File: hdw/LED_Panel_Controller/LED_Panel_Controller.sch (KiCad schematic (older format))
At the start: 0 parts

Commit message: lots of schematic progress
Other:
- note added: "14. Platform ETC"
- note removed: "14. Time of Flight"
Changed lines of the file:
@@
 encoding utf-8
 Sheet 1 34
-Title ""
-Date "2020-09-08"
-Rev ""
-Comp ""
+Title "LED Panel Controller"
+Date "2020-12-23"
+Rev "A"
+Comp "Drew Maatman, Logan Wedel"
 Comment1 ""
 Comment2 ""
@@
 S 3750 5420 500  150
 U 5F582A92
-F0 "Time of Flight" 50
-F1 "Time_of_Flight.sch" 50
+F0 "Platform ETC" 50
+F1 "Platform_ETC.sch" 50
 $EndSheet
 $Sheet
@@
 13. I2C Boost
 Text Notes 1290 5570 0    100  ~ 20
-14. Time of Flight
+14. Platform ETC
 Text Notes 1290 5920 0    100  ~ 20
 15. USB UART Bridge

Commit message: made a lot more schematic progress
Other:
- note added: "TODO:\n- Determine actual +12V current draw, reevaluate input protection circuit - 2A\n- Determine image size, external flash size- 16,384 bytes\n* Figure out screen modes/mode LEDs\n* Draw WiFi module sheet\n* What PIC32MZ SKU will we use? Should be highest memory + speed - Drew\n"
- note removed: "TODO:\n- Determine actual +12V current draw, reevaluate input protection circuit - 2A\n- Input EMI filter? - Drew\n- Determine image size, external flash size- 16,384 bytes\n- Determine +5V current draw, decide on converter - Drew - 3A\n- Determine +3.3V Current Draw, decide on converter - Drew\n- Remove high frequency PIC32MZ bypass caps - Drew\n- Figure out panel connectors - Drew\n* Figure out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"
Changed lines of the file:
@@
 33. Mechanical
 Text Notes 8660 6640 0    50   ~ 0
-TODO:\n- Determine actual +12V current draw, reevaluate input protection circuit - 2A\n- Input EMI filter? - Drew\n- Determine image size, external flash size- 16,384 bytes\n- Determine +5V current draw, decide on converter - Drew - 3A\n- Determine +3.3V Current Draw, decide on converter - Drew\n- Remove high frequency PIC32MZ bypass caps - Drew\n- Figure out panel connectors - Drew\n* Figure out panel level shifting - Logan\n- Figure out SPI flash circuit - Drew\n* Figure out screen modes/mode LEDs\n- Draw SD card sheet - Logan\n* Draw WiFi module sheet\n- Draw I2C boost sheet with LTC1694 - Drew\n* Determine what will be configurable, add hardstraps\n* What will pushbuttons do?\n* What PIC32MZ SKU will we use? Should be highest memory + speed - Drew\n- Change PGOOD LEDs sheet to use +3.3V_PGL global power symbol - Drew\n* Add USB Telemetry sheet\n
+TODO:\n- Determine actual +12V current draw, reevaluate input protection circuit - 2A\n- Determine image size, external flash size- 16,384 bytes\n* Figure out screen modes/mode LEDs\n* Draw WiFi module sheet\n* What PIC32MZ SKU will we use? Should be highest memory + speed - Drew\n
 $Sheet
 S 7030 5770 500  150

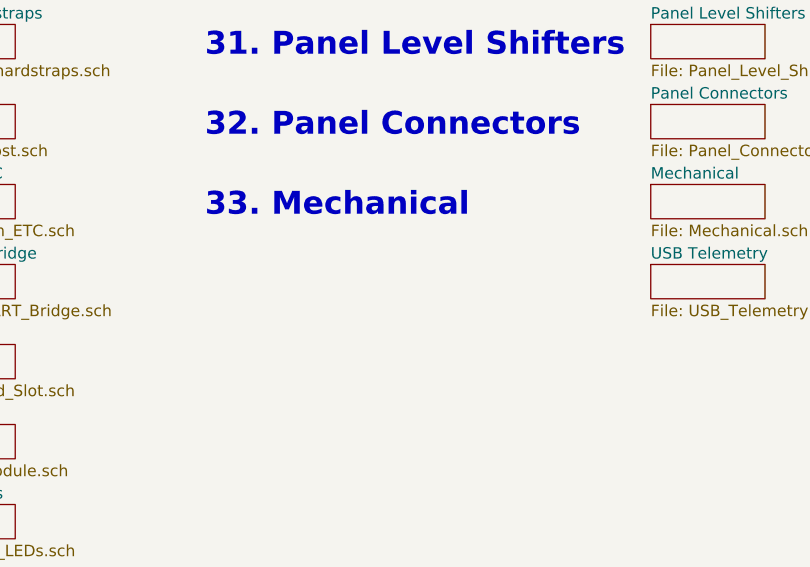
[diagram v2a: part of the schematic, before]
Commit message: fixed level shifter sheet
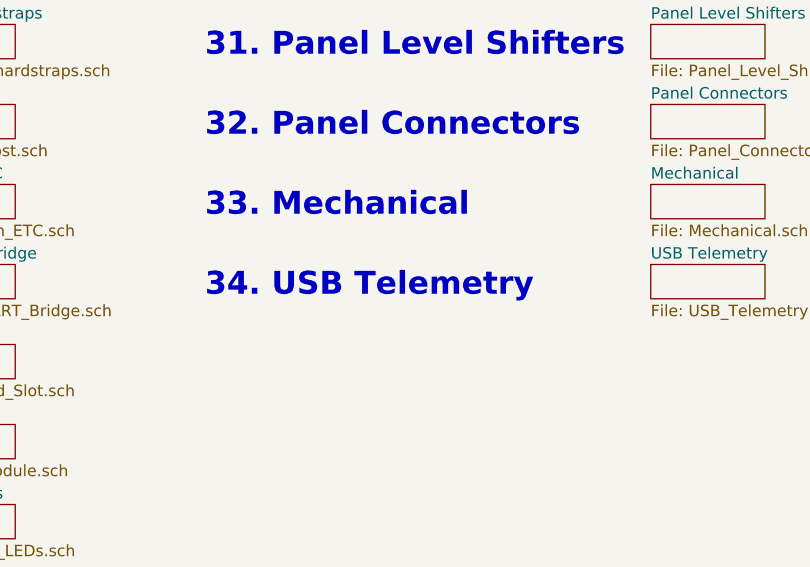
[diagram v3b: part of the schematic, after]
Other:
- note added: "34. USB Telemetry"
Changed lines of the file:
@@
 F1 "USB_Telemetry.sch" 50
 $EndSheet
+Text Notes 5080 5920 0    100  ~ 20
+34. USB Telemetry
 $EndSCHEMATC

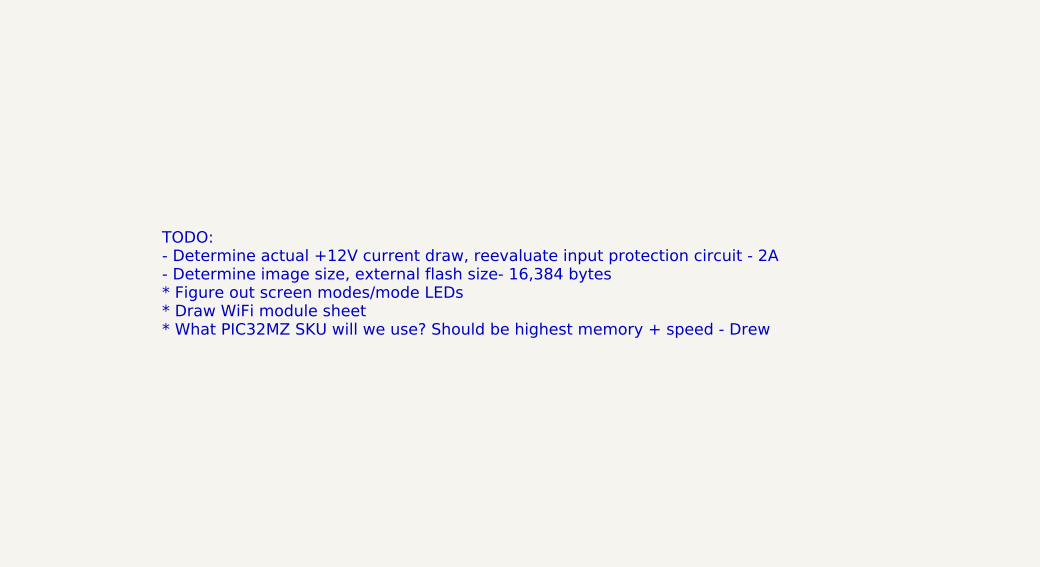
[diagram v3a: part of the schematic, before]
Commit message: lots of MCU pin assignments
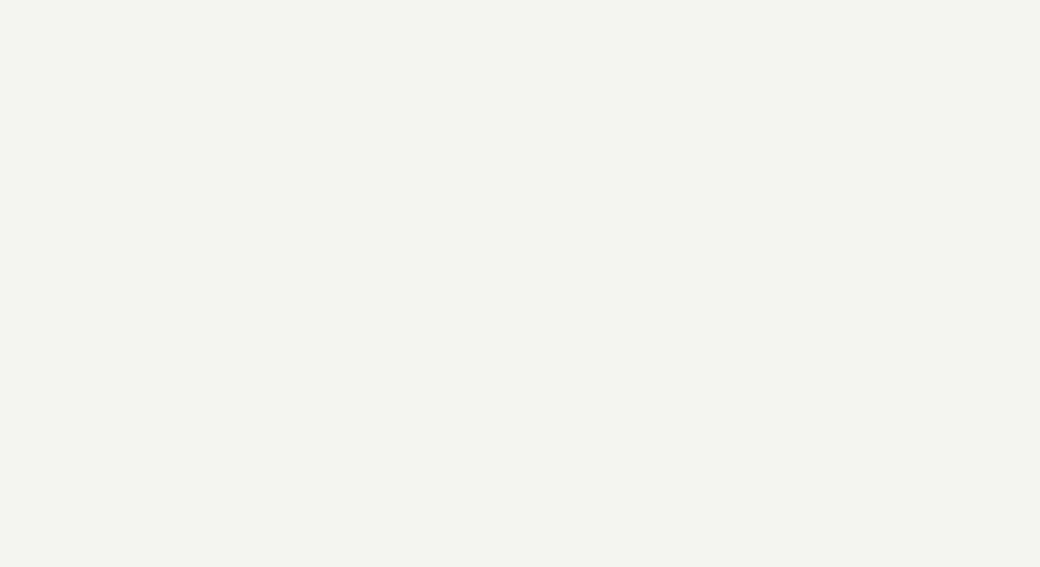
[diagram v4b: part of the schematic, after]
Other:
- note removed: "TODO:\n- Determine actual +12V current draw, reevaluate input protection circuit - 2A\n- Determine image size, external flash size- 16,384 bytes\n* Figure out screen modes/mode LEDs\n* Draw WiFi module sheet\n* What PIC32MZ SKU will we use? Should be highest memory + speed - Drew\n"
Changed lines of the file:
@@
 Text Notes 5080 5570 0    100  ~ 20
 33. Mechanical
-Text Notes 8660 6640 0    50   ~ 0
-TODO:\n- Determine actual +12V current draw, reevaluate input protection circuit - 2A\n- Determine image size, external flash size- 16,384 bytes\n* Figure out screen modes/mode LEDs\n* Draw WiFi module sheet\n* What PIC32MZ SKU will we use? Should be highest memory + speed - Drew\n
 $Sheet
 S 7030 5770 500  150

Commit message: more schematic development
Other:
- note added: "16. USB Telemetry"
- note added: "17. SD Card Slot"
- note added: "18. WiFi Module"
- note added: "19. PGOOD LEDs"
- note added: "20. Status LEDs"
- note added: "21. Backup RTC"
- note added: "22. Pushbuttons"
- note added: "23. Mode LEDs"
- note added: "24. SPI Flash 0"
- note added: "25. SPI Flash 1"
- note added: "26. SPI Flash 2"
- note added: "27. SPI Flash 3"
- note added: "28. SPI Flash 4"
- note added: "29. SPI Flash 5"
- note added: "30. SPI Flash 6"
- note added: "31. SPI Flash 7"
- note added: "32. Panel Level Shifters"
- note added: "33. Panel Connectors"
- note added: "34. Mechanical"
- note removed: "16. SD Card Slot"
- note removed: "17. WiFi Module"
- note removed: "18. PGOOD LEDs"
- note removed: "19. Status LEDs"
- note removed: "20. Backup RTC"
- note removed: "21. Pushbuttons"
- note removed: "22. Mode LEDs"
- note removed: "23. SPI Flash 0"
- note removed: "24. SPI Flash 1"
- note removed: "25. SPI Flash 2"
- note removed: "26. SPI Flash 3"
- note removed: "27. SPI Flash 4"
- note removed: "28. SPI Flash 5"
- note removed: "29. SPI Flash 6"
- note removed: "30. SPI Flash 7"
- note removed: "31. Panel Level Shifters"
- note removed: "32. Panel Connectors"
- note removed: "33. Mechanical"
- note removed: "34. USB Telemetry"
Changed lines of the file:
@@
 Sheet 1 34
 Title "LED Panel Controller"
-Date "2020-12-23"
+Date "2021-03-24"
 Rev "A"
-Comp "Drew Maatman, Logan Wedel"
+Comp "Drew Maatman"
 Comment1 ""
 Comment2 ""
@@
 $Sheet
 S 3750 6120 500  150
+U 5F7B4289
+F0 "USB Telemetry" 50
+F1 "USB_Telemetry.sch" 50
+$EndSheet
+$Sheet
+S 3750 6470 500  150
 U 5F582E11
 F0 "SD Card Slot" 50
@@
 $EndSheet
 $Sheet
-S 3750 6470 500  150
+S 3750 6820 500  150
 U 5F582E44
 F0 "WiFi Module" 50
@@
 $EndSheet
 $Sheet
-S 3750 6820 500  150
+S 3750 7170 500  150
 U 5F582E4A
 F0 "PGOOD LEDs" 50
@@
 $EndSheet
 $Sheet
-S 3750 7170 500  150
+S 3750 7520 500  150
 U 5F582E50
 F0 "Status LEDs" 50
@@
 $EndSheet
 $Sheet
-S 3750 7520 500  150
+S 7030 1220 500  150
 U 5F582E7C
 F0 "Backup RTC" 50
@@
 Text Notes 1290 5920 0    100  ~ 20
 15. USB UART Bridge
-Text Notes 1290 6270 0    100  ~ 20
-16. SD Card Slot
 Text Notes 1290 6620 0    100  ~ 20
-17. WiFi Module
+17. SD Card Slot
 Text Notes 1290 6970 0    100  ~ 20
-18. PGOOD LEDs
+18. WiFi Module
 Text Notes 1290 7320 0    100  ~ 20
-19. Status LEDs
+19. PGOOD LEDs
 Text Notes 1290 7670 0    100  ~ 20
-20. Backup RTC
+20. Status LEDs
+Text Notes 5080 1370 0    100  ~ 20
+21. Backup RTC
 Text Notes 1290 1010 0    100  ~ 20
 01. Table of Contents
 $Sheet
-S 7030 1220 500  150
+S 7030 1570 500  150
 U 5F58356B
 F0 "Pushbuttons" 50
@@
 $EndSheet
 $Sheet
-S 7030 1570 500  150
+S 7030 1920 500  150
 U 5F583571
 F0 "Mode LEDs" 50
@@
 $EndSheet
 $Sheet
-S 7030 1920 500  150
+S 7030 2270 500  150
 U 5F583577
 F0 "SPI Flash 0" 50
@@
 $EndSheet
 $Sheet
-S 7030 2270 500  150
+S 7030 2620 500  150
 U 5F58358C
 F0 "SPI Flash 1" 50
@@
 $EndSheet
 $Sheet
-S 7030 2620 500  150
+S 7030 2970 500  150
 U 5F583592
 F0 "SPI Flash 2" 50
@@
 $EndSheet
 $Sheet
-S 7030 2970 500  150
+S 7030 3320 500  150
 U 5F583598
 F0 "SPI Flash 3" 50
@@
 $EndSheet
 $Sheet
-S 7030 3320 500  150
+S 7030 3670 500  150
 U 5F58359E
 F0 "SPI Flash 4" 50
@@
 $EndSheet
 $Sheet
-S 7030 3670 500  150
+S 7030 4020 500  150
 U 5F5835A4
 F0 "SPI Flash 5" 50
@@
 $EndSheet
 $Sheet
-S 7030 4020 500  150
+S 7030 4370 500  150
 U 5F5835AA
 F0 "SPI Flash 6" 50
@@
 $EndSheet
 $Sheet
-S 7030 4370 500  150
+S 7030 4720 500  150
 U 5F5835B0
 F0 "SPI Flash 7" 50
 F1 "SPI_Flash_7.sch" 50
 $EndSheet
-Text Notes 5080 1370 0    100  ~ 20
-21. Pushbuttons
 Text Notes 5080 1720 0    100  ~ 20
-22. Mode LEDs
+22. Pushbuttons
 Text Notes 5080 2070 0    100  ~ 20
-23. SPI Flash 0
+23. Mode LEDs
 Text Notes 5080 2420 0    100  ~ 20
-24. SPI Flash 1
+24. SPI Flash 0
 Text Notes 5080 2770 0    100  ~ 20
-25. SPI Flash 2
+25. SPI Flash 1
 Text Notes 5080 3120 0    100  ~ 20
-26. SPI Flash 3
+26. SPI Flash 2
 Text Notes 5080 3470 0    100  ~ 20
-27. SPI Flash 4
+27. SPI Flash 3
 Text Notes 5080 3820 0    100  ~ 20
-28. SPI Flash 5
+28. SPI Flash 4
 Text Notes 5080 4170 0    100  ~ 20
-29. SPI Flash 6
+29. SPI Flash 5
 Text Notes 5080 4520 0    100  ~ 20
-30. SPI Flash 7
-$Sheet
-S 7030 4720 500  150
+30. SPI Flash 6
+Text Notes 5080 4870 0    100  ~ 20
+31. SPI Flash 7
+$Sheet
+S 7030 5070 500  150
 U 5F583BF6
 F0 "Panel Level Shifters" 50
@@
 $EndSheet
 $Sheet
-S 7030 5070 500  150
+S 7030 5420 500  150
 U 5F583BFC
 F0 "Panel Connectors" 50
@@
 $EndSheet
 $Sheet
-S 7030 5420 500  150
+S 7030 5770 500  150
 U 5F583C02
 F0 "Mechanical" 50
 F1 "Mechanical.sch" 50
 $EndSheet
-Text Notes 5080 4870 0    100  ~ 20
-31. Panel Level Shifters
 Text Notes 5080 5220 0    100  ~ 20
-32. Panel Connectors
+32. Panel Level Shifters
 Text Notes 5080 5570 0    100  ~ 20
-33. Mechanical
-$Sheet
-S 7030 5770 500  150
-U 5F7B4289
-F0 "USB Telemetry" 50
-F1 "USB_Telemetry.sch" 50
-$EndSheet
+33. Panel Connectors
 Text Notes 5080 5920 0    100  ~ 20
-34. USB Telemetry
+34. Mechanical
+Text Notes 1290 6270 0    100  ~ 20
+16. USB Telemetry
 $EndSCHEMATC

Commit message: having a mid-project crisis
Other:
- note added: "18. MLVDS Port"
- note removed: "18. WiFi Module"
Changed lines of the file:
@@
 S 3750 6820 500  150
 U 5F582E44
-F0 "WiFi Module" 50
-F1 "WiFi_Module.sch" 50
+F0 "MLVDS Port" 50
+F1 "MLVDS_Port.sch" 50
 $EndSheet
 $Sheet
@@
 17. SD Card Slot
 Text Notes 1290 6970 0    100  ~ 20
-18. WiFi Module
+18. MLVDS Port
 Text Notes 1290 7320 0    100  ~ 20
 19. PGOOD LEDs
